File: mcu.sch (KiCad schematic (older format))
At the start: 39 parts

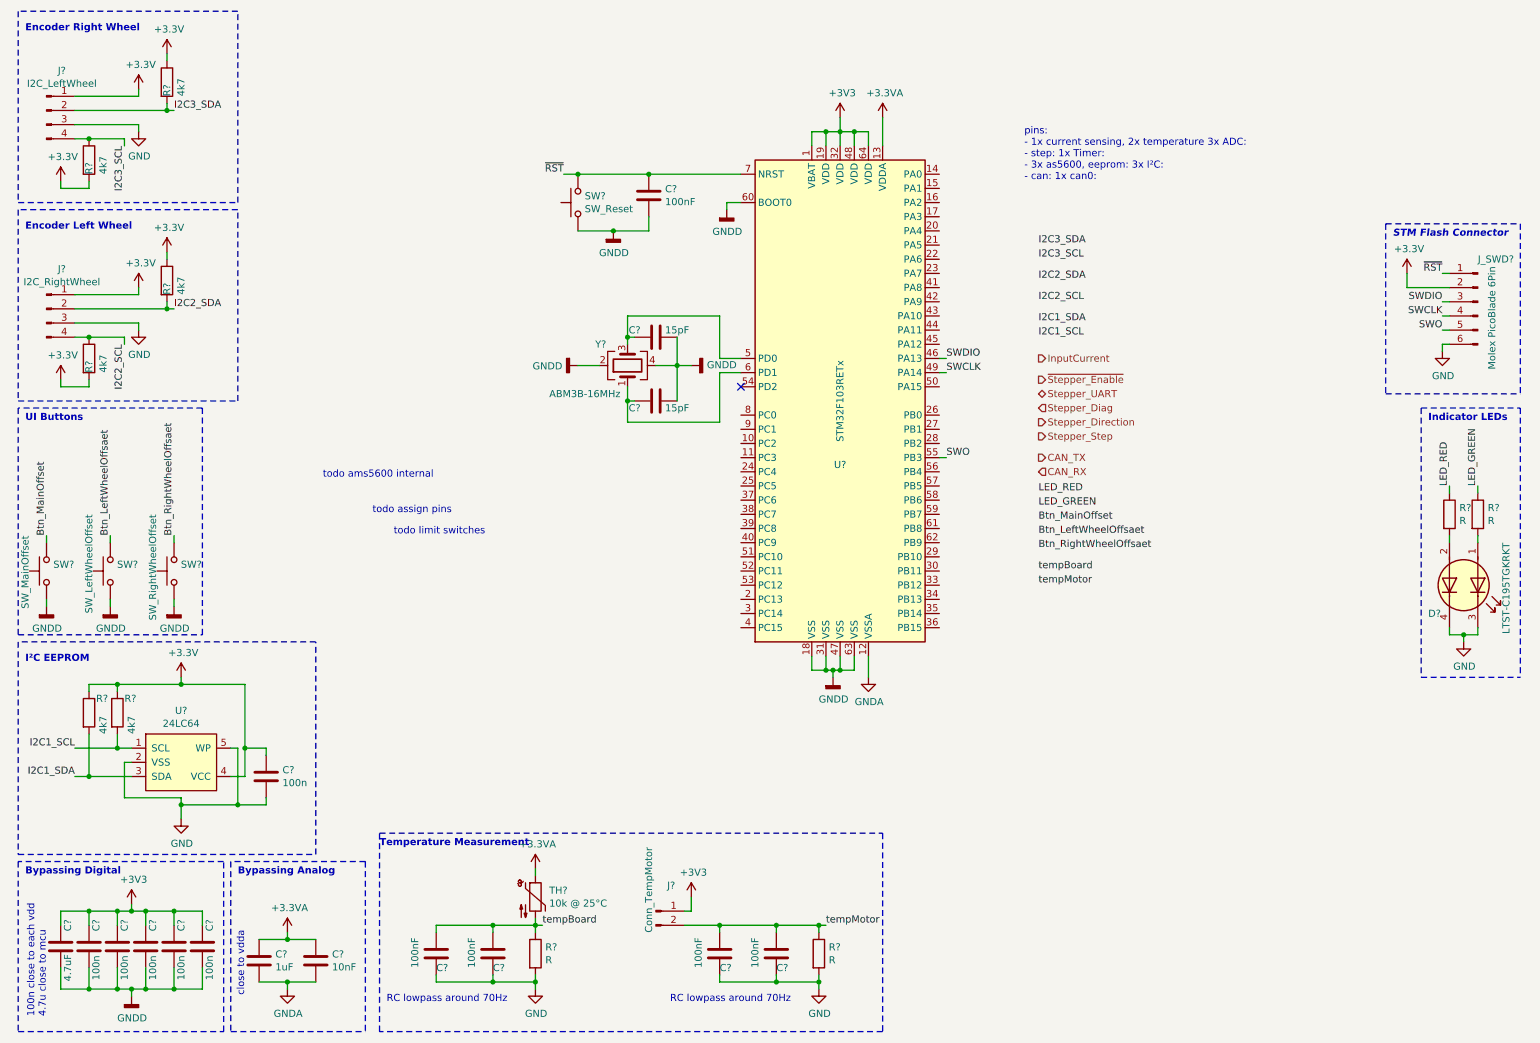
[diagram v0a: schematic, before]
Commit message: Specified dual led resistors Consolidated all grounds to just gnd Consolidated all 3.3 rails to just 3.3V Removed right endstop Removed right wheel angle, servo angle calibration button
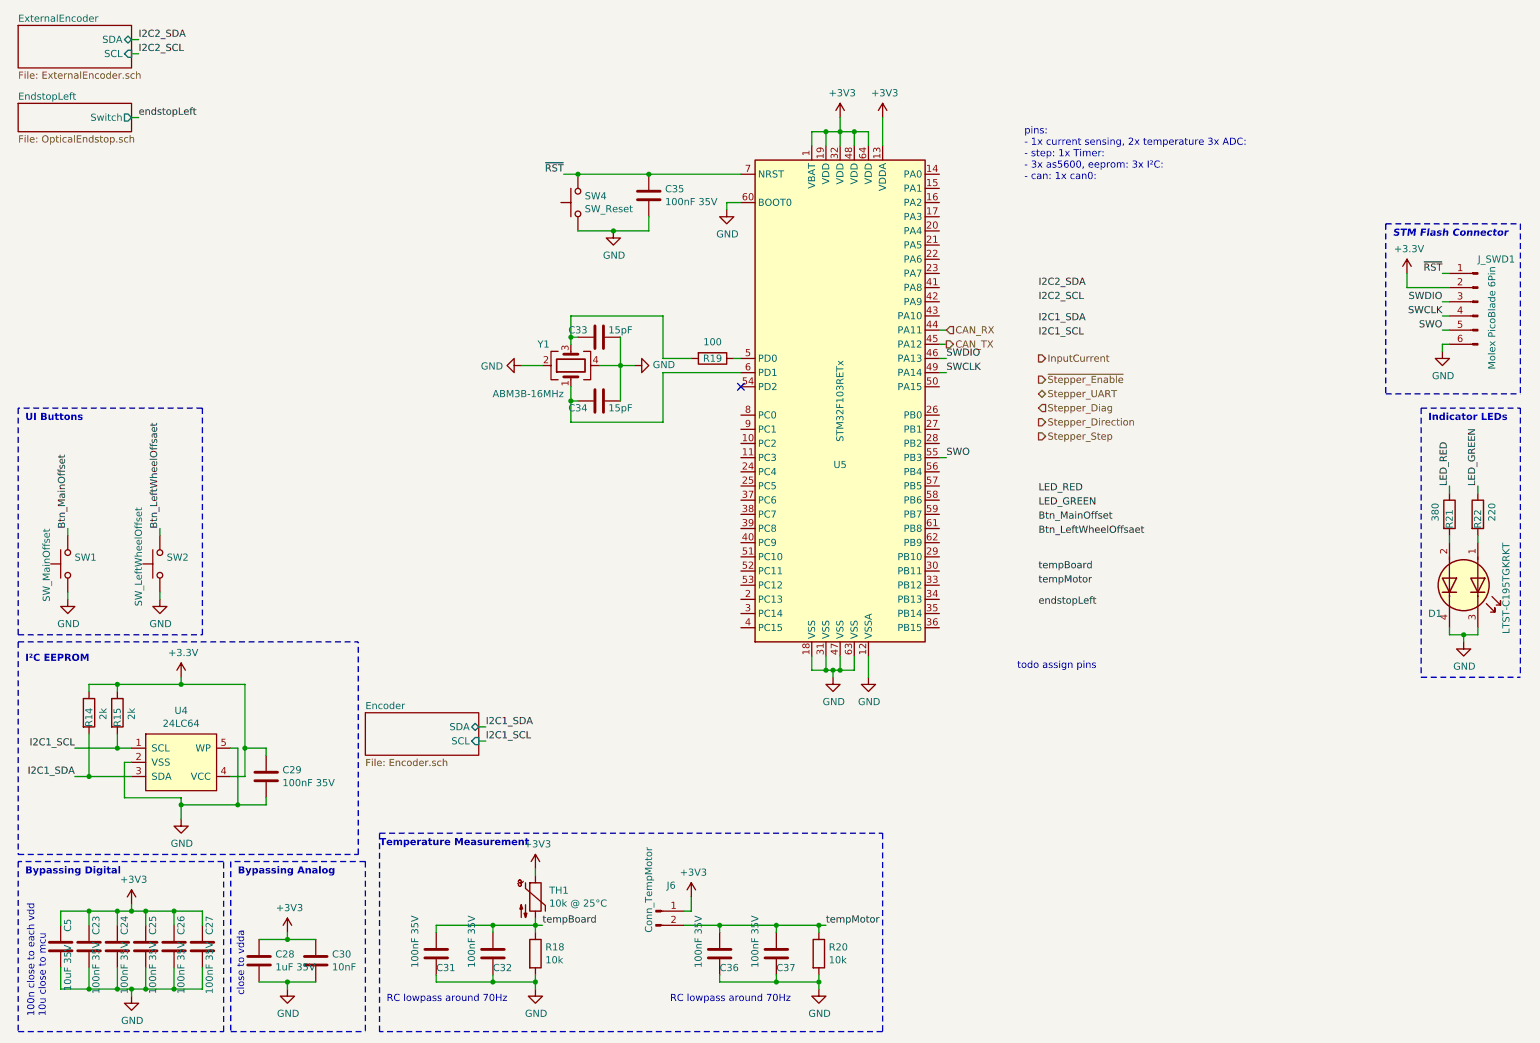
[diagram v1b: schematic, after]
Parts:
- removed J?: I2C_RightWheel, symbol Connector:Conn_01x04_Male
- removed J?: I2C_LeftWheel, symbol Connector:Conn_01x04_Male
- removed R? (x4): 4k7, Resistor_SMD:R_0603_1608Metric, symbol Device:R
- removed SW?: SW_RightWheelOffset, standardContent:SW_SPST_PTS636_SM25F, symbol Switch:SW_Push
- added R19: 100, Resistor_SMD:R_0603_1608Metric, symbol Device:R
- C23, C24, C25, C26, C27: renamed from C?; value 100n -> 100nF 35V; footprint (none) -> Capacitor_SMD:C_0603_1608Metric
- C28: renamed from C?; value 1uF -> 1uF 35V; footprint (none) -> Capacitor_SMD:C_0603_1608Metric
- C29: renamed from C?; value 100n -> 100nF 35V
- C30, C33, C34: renamed from C?; footprint (none) -> Capacitor_SMD:C_0603_1608Metric
- C31, C32, C35, C36, C37: renamed from C?; value 100nF -> 100nF 35V; footprint (none) -> Capacitor_SMD:C_0603_1608Metric
- C5: renamed from C?; value 4.7uF -> 10uF 35V; footprint (none) -> Capacitor_SMD:C_1206_3216Metric
- J6: renamed from J?; footprint (none) -> Connector_Molex:Molex_PicoBlade_53047-0210_1x02_P1.25mm_Vertical
- R14, R15: renamed from R?; value 4k7 -> 2k
- R18, R20: renamed from R?; value R -> 10k; footprint (none) -> Resistor_SMD:R_0603_1608Metric
- R21: renamed from R?; value R -> 380
- R22: renamed from R?; value R -> 220
- TH1: renamed from TH?; footprint (none) -> Resistor_SMD:R_0603_1608Metric
- gave numbers to parts that had none: 8
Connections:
- net +3.3VA is gone; now on net +3V3: C28.1, C30.1, TH1.1, U5.13 (VDDA)
- net GNDA is gone; now on net GND: C28.2, C30.2, U5.12 (VSSA)
- net GNDD is gone; now on net GND: C23.1, C24.1, C25.1, C26.1, C27.1, C33.1, C34.1, C35.2, C5.1, SW1.1, SW2.1, SW4.1, U5.18 (VSS), U5.31 (VSS), U5.47 (VSS), U5.60 (BOOT0), U5.63 (VSS), Y1.2, Y1.4
- net CAN_RX: now also U5.44 (PA11)
- net CAN_TX: now also U5.45 (PA12)
- net at C33.2, Y1.3: now also R19.2; no longer U5.5 (PD0)
- new net: R19.1, U5.5 (PD0)
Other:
- note added: "100n close to each vdd\n10u close to mcu"
- note removed: "100n close to each vdd\n4.7u close to mcu"
- note removed: "Encoder Left Wheel"
- note removed: "Encoder Right Wheel"
- note removed: "todo ams5600 internal"
- note removed: "todo limit switches"
- moved on the sheet: C33, C34, SW1, SW2, Y1

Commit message: Renamed ui buttons for better clarity
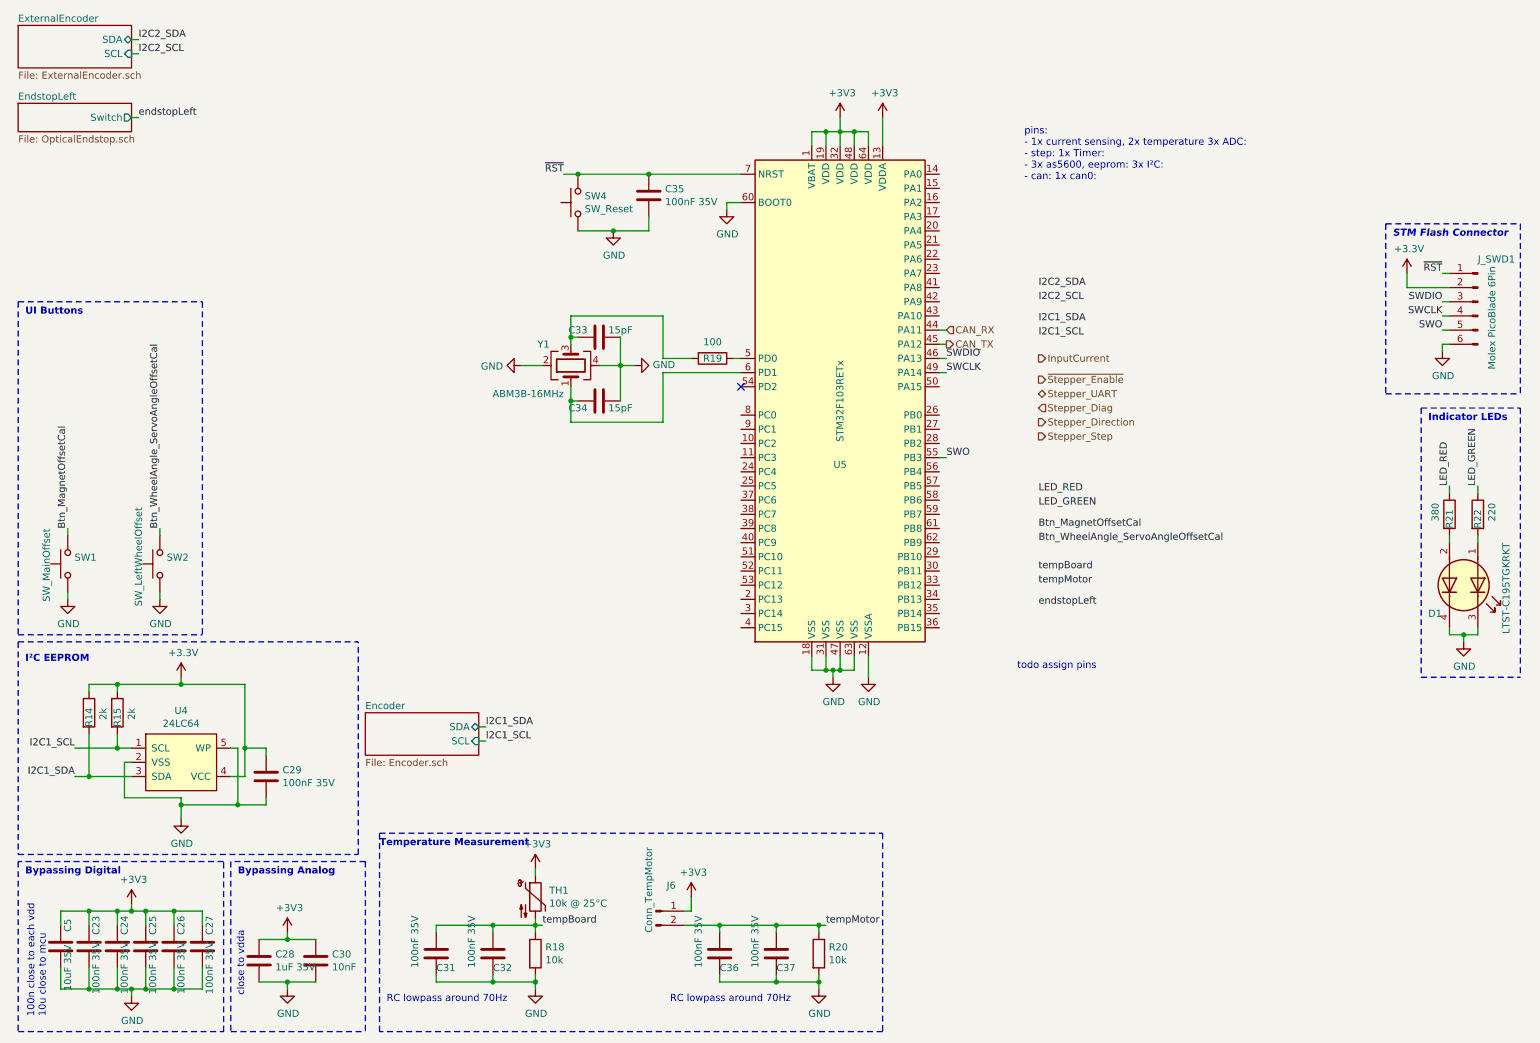
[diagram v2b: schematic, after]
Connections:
- net Btn_LeftWheelOffsaet renamed Btn_WheelAngle_ServoAngleOffsetCal
- net Btn_MainOffset renamed Btn_MagnetOffsetCal
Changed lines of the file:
@@
 	900  4200 900  4150
 Text Label 900  4150 1    50   ~ 0
-Btn_MainOffset
+Btn_MagnetOffsetCal
 Text Label 1550 4150 1    50   ~ 0
-Btn_LeftWheelOffsaet
+Btn_WheelAngle_ServoAngleOffsetCal
 Wire Wire Line
 	1550 4200 1550 4150
@@
 Text Label 7750 4000 0    50   ~ 0
 LED_GREEN
-Text Label 7750 4100 0    50   ~ 0
-Btn_MainOffset
-Text Label 7750 4200 0    50   ~ 0
-Btn_LeftWheelOffsaet
 Text Label 7100 3650 0    50   ~ 0
 SWO
@@
 I2C2_SDA
 Wire Notes Line
-	550  3300 550  4900
-Wire Notes Line
 	550  4900 1850 4900
-Wire Notes Line
-	1850 4900 1850 3300
-Wire Notes Line
-	1850 3300 550  3300
-Text Notes 600  3400 0    50   ~ 10
+Text Notes 600  2650 0    50   ~ 10
 UI Buttons
 Text Notes 600  6600 0    50   ~ 10
@@
 	0    -1   -1   0
 $EndComp
+Wire Notes Line
+	550  2550 1850 2550
+Wire Notes Line
+	550  2550 550  4900
+Wire Notes Line
+	1850 2550 1850 4900
+Text Label 7750 4250 0    50   ~ 0
+Btn_WheelAngle_ServoAngleOffsetCal
+Text Label 7750 4150 0    50   ~ 0
+Btn_MagnetOffsetCal
 $EndSCHEMATC

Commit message: wip layout
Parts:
- removed C29, C31, C32, C36, C37: 100nF 35V, Capacitor_SMD:C_0603_1608Metric, symbol Device:C
- removed R18: 10k, Resistor_SMD:R_0603_1608Metric, symbol Device:R
- removed SW1: SW_MainOffset, standardContent:SW_SPST_PTS636_SM25F, symbol Switch:SW_Push
- removed SW2: SW_LeftWheelOffset, standardContent:SW_SPST_PTS636_SM25F, symbol Switch:SW_Push
- removed TH1: 10k @ 25°C, Resistor_SMD:R_0603_1608Metric, symbol Device:Thermistor_NTC
- removed U4: 24LC64, Package_TO_SOT_SMD:SOT-23-5, symbol standardContent:24LC64
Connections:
- net I2C1_SCL: now also U5.58 (PB6)
- net I2C1_SDA: now also U5.59 (PB7)
- net I2C2_SCL: now also U5.29 (PB10)
- net I2C2_SDA: now also U5.30 (PB11)
- net LED_GREEN: now also U5.15 (PA1)
- net LED_RED: now also U5.16 (PA2)
- net Stepper_Direction: now also U5.51 (PC10)
- net Stepper_Step: now also U5.50 (PA15)
- net endstopRight: now reaches U5.2 (PC13)
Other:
- note removed: "I²C EEPROM"
- note removed: "RC lowpass around 70Hz"
- note removed: "UI Buttons"
- moved on the sheet: R14, R15

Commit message: Finished v1 layout Added pictures to readme
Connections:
- net InputCurrent: now also U5.23 (PA7)
- net Stepper_Diag: now also U5.3 (PC14)
- net Stepper_UART: now also U5.53 (PC12)
- net tempMotor: now also U5.24 (PC4)
- net ~Stepper_Enable: now also U5.4 (PC15)
- no-connect marks 1 -> 30
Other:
- note removed: "pins:\n- 1x current sensing, 2x temperature 3x ADC:\n- step: 1x Timer: \n- 3x as5600, eeprom: 3x I²C:\n- can: 1x can0:\n"
- note removed: "todo assign pins"
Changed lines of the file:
@@
 Wire Notes Line
 	10450 3300 11150 3300
-Text Notes 7650 1700 0    50   ~ 0
-pins:\n- 1x current sensing, 2x temperature 3x ADC:\n- step: 1x Timer: \n- 3x as5600, eeprom: 3x I²C:\n- can: 1x can0:\n
 Wire Notes Line
 	550  6500 550  7700
@@
 Wire Notes Line
 	3100 7700 3100 6300
-Text Label 7750 4550 0    50   ~ 0
+Text Label 5600 3750 2    50   ~ 0
 tempMotor
 Text HLabel 7100 2750 2    50   Input ~ 0
@@
 Text HLabel 5600 4350 0    50   Output ~ 0
 Stepper_Direction
-Text HLabel 7750 3300 2    50   Input ~ 0
+Text HLabel 5600 4750 0    50   Input ~ 0
 Stepper_Diag
-Text HLabel 7750 3200 2    50   BiDi ~ 0
+Text HLabel 5600 4550 0    50   BiDi ~ 0
 Stepper_UART
-Text HLabel 7750 3100 2    50   Output ~ 0
+Text HLabel 5600 4850 0    50   Output ~ 0
 ~Stepper_Enable
-Text HLabel 7750 2950 2    50   Output ~ 0
+Text HLabel 7100 2350 2    50   Input ~ 0
 InputCurrent
 Text Label 7100 3950 0    50   ~ 0
@@
 Text Notes 3100 6400 0    50   ~ 10
 Temperature Measurement
-Text Notes 7600 5150 0    50   ~ 0
-todo assign pins
 $Comp
 L Device:R R19
@@
 Wire Wire Line
 	5600 4650 5650 4650
+Wire Wire Line
+	7100 2350 7050 2350
+Wire Wire Line
+	5600 3750 5650 3750
+Wire Wire Line
+	5600 4550 5650 4550
+Wire Wire Line
+	5600 4750 5650 4750
+Wire Wire Line
+	5600 4850 5650 4850
+NoConn ~ 7050 4850
+NoConn ~ 7050 4750
+NoConn ~ 7050 4650
+NoConn ~ 7050 4550
+NoConn ~ 7050 4250
+NoConn ~ 7050 4150
+NoConn ~ 7050 3850
+NoConn ~ 7050 3750
+NoConn ~ 7050 3550
+NoConn ~ 7050 3450
+NoConn ~ 7050 3350
+NoConn ~ 7050 2650
+NoConn ~ 7050 2550
+NoConn ~ 7050 2450
+NoConn ~ 7050 2250
+NoConn ~ 7050 2150
+NoConn ~ 7050 2050
+NoConn ~ 7050 1950
+NoConn ~ 5650 3350
+NoConn ~ 5650 3450
+NoConn ~ 5650 3550
+NoConn ~ 5650 3650
+NoConn ~ 5650 3850
+NoConn ~ 5650 3950
+NoConn ~ 5650 4050
+NoConn ~ 5650 4150
+NoConn ~ 5650 4250
+NoConn ~ 5650 4450
+NoConn ~ 7050 1650
 $EndSCHEMATC
